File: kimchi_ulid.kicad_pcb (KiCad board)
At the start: 4 copper layers, 65 x 32 mm, 10 parts, among them J1 DF40HC(3.5)-60DS, J2 DF40HC(3.5)-60DS, K1 KIMCHI_MICRO, U1 24C32

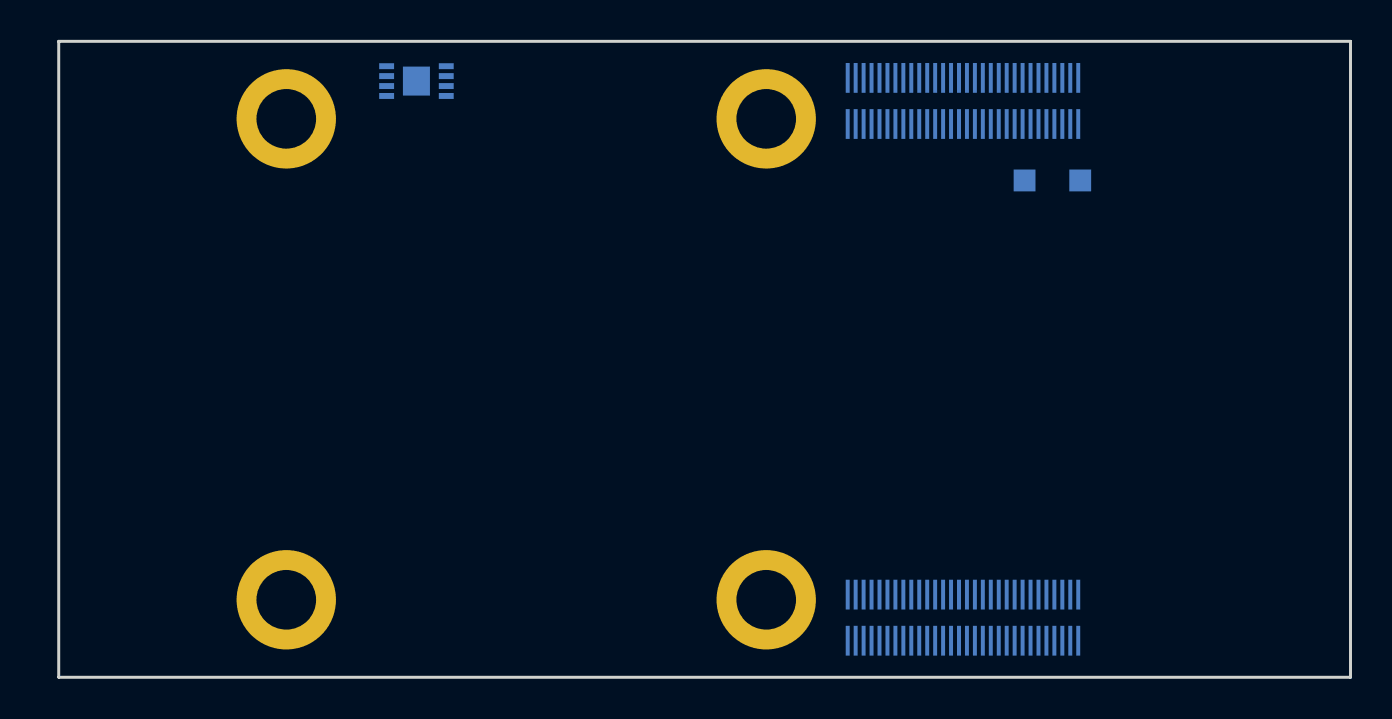
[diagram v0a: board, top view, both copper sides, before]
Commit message: Initial work on design
- Update symbols to KiCad v6
- Start inital placement and routing of design
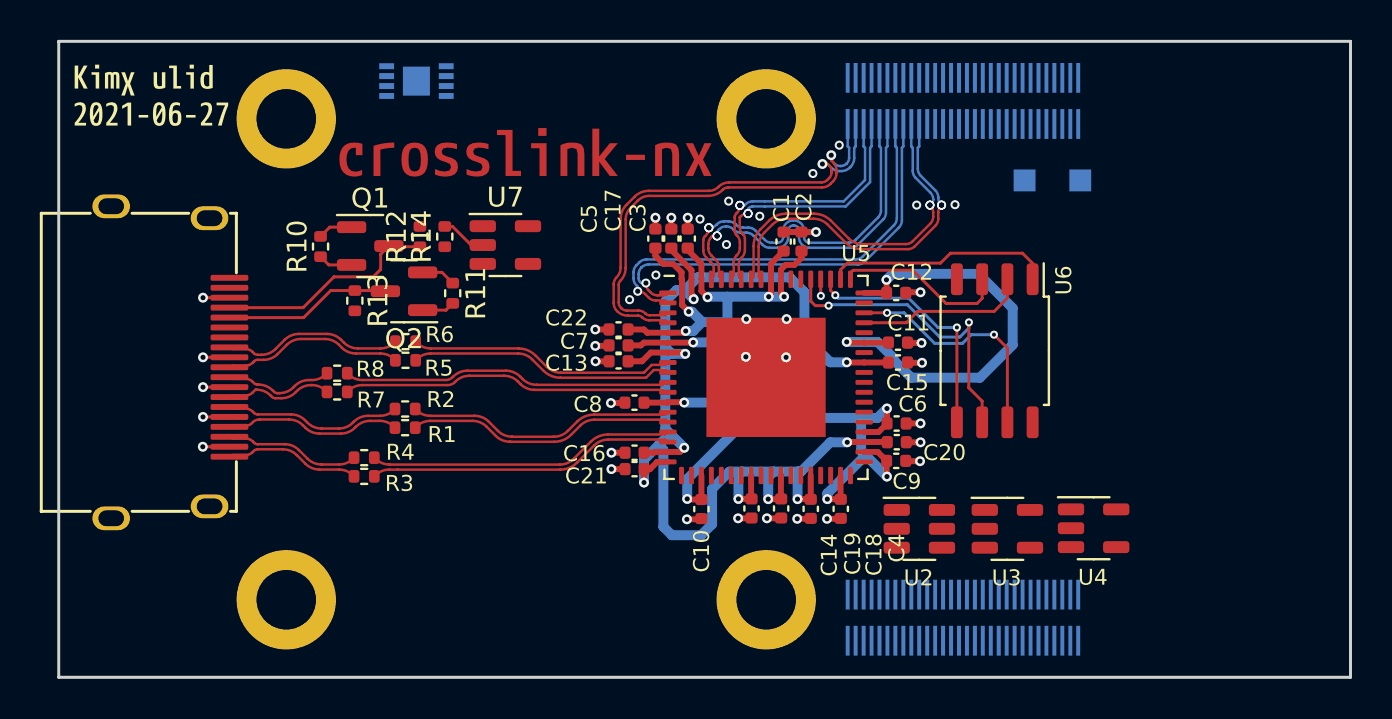
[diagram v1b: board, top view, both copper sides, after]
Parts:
- added C1: 0.1uF, Capacitor_SMD:C_0402_1005Metric, F.Cu at (143.5, 104.1)
- added C10: 0.1uF, Capacitor_SMD:C_0402_1005Metric, F.Cu at (139.3, 117.5)
- added C11: 0.1uF, Capacitor_SMD:C_0402_1005Metric, F.Cu at (149.2, 109.2)
- added C12: 0.1uF, Capacitor_SMD:C_0402_1005Metric, F.Cu at (149.1, 106.7)
- added C13: 0.1uF, Capacitor_SMD:C_0402_1005Metric, F.Cu at (135.2, 110.1)
- added C14: 0.1uF, Capacitor_SMD:C_0402_1005Metric, F.Cu at (141.9, 117.5)
- added C15: 0.1uF, Capacitor_SMD:C_0402_1005Metric, F.Cu at (149.2, 110.2)
- added C16: 0.1uF, Capacitor_SMD:C_0402_1005Metric, F.Cu at (136.0, 114.7)
- added C17: 0.1uF, Capacitor_SMD:C_0402_1005Metric, F.Cu at (137.8, 103.9)
- added C18: 0.1uF, Capacitor_SMD:C_0402_1005Metric, F.Cu at (144.8, 117.5)
- added C19: 0.1uF, Capacitor_SMD:C_0402_1005Metric, F.Cu at (143.3, 117.5)
- added C2: 0.1uF, Capacitor_SMD:C_0402_1005Metric, F.Cu at (144.4, 104.1)
- added C20: 0.1uF, Capacitor_SMD:C_0402_1005Metric, F.Cu at (149.2, 114.2)
- added C21: 0.1uF, Capacitor_SMD:C_0402_1005Metric, F.Cu at (136.0, 115.5)
- added C22: 0.1uF, Capacitor_SMD:C_0402_1005Metric, F.Cu at (135.2, 108.5)
- added C3: 0.1uF, Capacitor_SMD:C_0402_1005Metric, F.Cu at (138.7, 103.9)
- added C4: 0.1uF, Capacitor_SMD:C_0402_1005Metric, F.Cu at (146.3, 117.5)
- added C5: 0.1uF, Capacitor_SMD:C_0402_1005Metric, F.Cu at (137.0, 103.9)
- added C6: 0.1uF, Capacitor_SMD:C_0402_1005Metric, F.Cu at (149.2, 113.2)
- added C7: 0.1uF, Capacitor_SMD:C_0402_1005Metric, F.Cu at (135.2, 109.3)
- added C8: 0.1uF, Capacitor_SMD:C_0402_1005Metric, F.Cu at (136.0, 112.2)
- added C9: 0.1uF, Capacitor_SMD:C_0402_1005Metric, F.Cu at (149.1, 115.1)
- added J3: HDMI_A_1.4, kimchi_ulid:HDMI-10029449-111RLF, F.Cu at (114.6, 110.2)
- added Q1: 2N7002, Package_TO_SOT_SMD:SOT-23, F.Cu at (122.7, 104.3)
- added Q2: 2N7002, Package_TO_SOT_SMD:SOT-23, F.Cu at (124.4, 106.6)
- added R1: R, Resistor_SMD:R_0402_1005Metric, F.Cu at (124.4, 113.4)
- added R10: 2k2, Resistor_SMD:R_0402_1005Metric, F.Cu at (120.2, 104.3)
- added R11: 2k2, Resistor_SMD:R_0402_1005Metric, F.Cu at (126.8, 106.7)
- added R12: 2k2, Resistor_SMD:R_0402_1005Metric, F.Cu at (125.2, 103.8)
- added R13: 2k2, Resistor_SMD:R_0402_1005Metric, F.Cu at (121.9, 107.0)
- added R14: 47k, Resistor_SMD:R_0402_1005Metric, F.Cu at (126.4, 103.8)
- added R2: R, Resistor_SMD:R_0402_1005Metric, F.Cu at (124.4, 112.5)
- added R3: R, Resistor_SMD:R_0402_1005Metric, F.Cu at (122.4, 115.9)
- added R4: R, Resistor_SMD:R_0402_1005Metric, F.Cu at (122.4, 115.0)
- added R5: R, Resistor_SMD:R_0402_1005Metric, F.Cu at (124.5, 110.0)
- added R6: R, Resistor_SMD:R_0402_1005Metric, F.Cu at (124.5, 109.1)
- added R7: R, Resistor_SMD:R_0402_1005Metric, F.Cu at (121.0, 111.6)
- added R8: R, Resistor_SMD:R_0402_1005Metric, F.Cu at (121.0, 110.7)
- added U2: LM3880, Package_TO_SOT_SMD:SOT-23-6, F.Cu at (150.3, 118.5)
- added U3: LD3985M27R_SOT23, Package_TO_SOT_SMD:SOT-23-5, F.Cu at (154.7, 118.5)
- added U4: LD3985M27R_SOT23, Package_TO_SOT_SMD:SOT-23-5, F.Cu at (159.1, 118.5)
- added U5: LIFCL40-NX, Package_DFN_QFN:QFN-72-1EP_10x10mm_P0.5mm_EP6x6mm, F.Cu at (142.6, 110.9)
- added U6: W25Q32JVSS, Package_SO:SOIC-8_5.23x5.23mm_P1.27mm, F.Cu at (154.1, 109.6)
- added U7: 74AUC1G17, Package_TO_SOT_SMD:SOT-23-5, F.Cu at (129.5, 104.2)
- added svg2mod: G***, svg2mod, F.Cu at (111.3, 96.0)
- added svg2mod: G***, svg2mod, F.Cu at (111.7, 97.7)
- added svg2mod: G***, svg2mod, F.Cu at (130.4, 99.8)
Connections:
- D1 pad 2: (no net) -> /VCHG_PROT
- J1 pad 1: (no net) -> /USDHC3_CMD
- J1 pad 11: (no net) -> unconnected-(J1-Pad11)
- J1 pad 17: (no net) -> I2C3_SDA
- J1 pad 18: (no net) -> I2C3_SCL
- J1 pad 19: (no net) -> I2C2_SDA
- J1 pad 2: (no net) -> /USDHC3_CLK
- J1 pad 20: (no net) -> I2C2_SCL
- J1 pad 21: (no net) -> I2C1_SDA
- J1 pad 22: (no net) -> I2C1_SCL
- J1 pad 23: (no net) -> ECSPI1_SCLK
- J1 pad 24: (no net) -> ECSPI1_SS0
- J1 pad 25: (no net) -> ECSPI1_MOSI
- J1 pad 26: (no net) -> ECSPI1_MISO
- J1 pad 27: (no net) -> ECSPI2_SCLK
- J1 pad 28: (no net) -> ECSPI2_SS0
- J1 pad 29: (no net) -> ECSPI2_MOSI
- J1 pad 3: (no net) -> /USDHC3_DATA3
- J1 pad 30: (no net) -> ECSPI2_MISO
- J1 pad 31: (no net) -> /DISP_D0_N
- J1 pad 32: (no net) -> /DISP_D0_P
- J1 pad 33: (no net) -> /DISP_D1_N
- J1 pad 34: (no net) -> /DISP_D1_P
- J1 pad 35: (no net) -> /DISP_CK_N
- J1 pad 36: (no net) -> /DISP_CK_P
- J1 pad 37: (no net) -> /DISP_D2_N
- J1 pad 38: (no net) -> /DISP_D2_P
- J1 pad 39: (no net) -> /DISP_D3_N
- J1 pad 4: (no net) -> /USDHC3_DATA0
- J1 pad 40: (no net) -> /DISP_D3_P
- J1 pad 41: (no net) -> /CAM_D0_N
- J1 pad 42: (no net) -> /CAM_D0_P
- J1 pad 43: (no net) -> /CAM_D1_N
- J1 pad 44: (no net) -> /CAM_D1_P
- J1 pad 45: (no net) -> /CAM_CK_N
- J1 pad 46: (no net) -> /CAM_CK_P
- J1 pad 47: (no net) -> /CAM_D2_N
- J1 pad 48: (no net) -> /CAM_D2_P
- J1 pad 49: (no net) -> /CAM_D3_N
- J1 pad 5: (no net) -> /USDHC3_DATA1
- J1 pad 50: (no net) -> /CAM_D3_P
- J1 pad 51: (no net) -> unconnected-(J1-Pad51)
- J1 pad 57: (no net) -> USB2_VBUS
- J1 pad 58: (no net) -> USB2_ID
- J1 pad 59: (no net) -> USB2_DN
- J1 pad 6: (no net) -> /USDHC3_DATA2
- J1 pad 60: (no net) -> USB2_DP
- J2 pad 1: (no net) -> /ENET_MDIO
- J2 pad 10: (no net) -> /ENET_TD0
- J2 pad 11: (no net) -> /ENET_TD3
- J2 pad 12: (no net) -> /ENET_TD2
- J2 pad 13: (no net) -> /ENET_TX_CTL
- J2 pad 14: (no net) -> /ENET_TXC
- J2 pad 15: (no net) -> SAI2_RXD0
- J2 pad 16: (no net) -> SAI2_TXFS
- J2 pad 17: (no net) -> SAI2_RXC
- J2 pad 18: (no net) -> SAI2_TXD0
- J2 pad 19: (no net) -> SAI2_TXC
- J2 pad 2: (no net) -> /ENET_MDC
- J2 pad 20: (no net) -> SAI2_MCLK
- J2 pad 21: (no net) -> SAI2_RXFS
- J2 pad 22: (no net) -> GPIO1[15]
- J2 pad 23: (no net) -> GPIO1[14]
- J2 pad 24: (no net) -> GPIO1[13]
- J2 pad 25: (no net) -> GPIO1[12]
- J2 pad 26: (no net) -> GPIO1[11]
- J2 pad 27: (no net) -> GPIO1[10]
- J2 pad 28: (no net) -> GPIO1[9]
- J2 pad 29: (no net) -> GPIO1[1]
- J2 pad 3: (no net) -> /ENET_RD3
- J2 pad 30: (no net) -> GPIO1[0]
- J2 pad 31: (no net) -> SAI3_TXC
- J2 pad 32: (no net) -> SAI3_TXD
- J2 pad 33: (no net) -> SAI3_RXD
- J2 pad 34: (no net) -> SAI3_RXFS
- J2 pad 35: (no net) -> SAI3_RXC
- J2 pad 36: (no net) -> SAI3_TXFS
- J2 pad 37: (no net) -> SAI3_MCLK
- J2 pad 4: (no net) -> /ENET_RD1
- J2 pad 42: (no net) -> unconnected-(J2-Pad42)
- J2 pad 46: (no net) -> UART1_TX
- J2 pad 47: (no net) -> UART1_RX
- J2 pad 48: (no net) -> UART3_TX
- J2 pad 49: (no net) -> UART3_RX
- J2 pad 5: (no net) -> /ENET_RD2
- J2 pad 54: (no net) -> unconnected-(J2-Pad54)
- J2 pad 58: (no net) -> unconnected-(J2-Pad58)
- J2 pad 59: (no net) -> PCIE_USB_D_P
- J2 pad 6: (no net) -> /ENET_RD0
- J2 pad 60: (no net) -> PCIE_USB_D_N
- J2 pad 7: (no net) -> /ENET_RXC
- J2 pad 8: (no net) -> /ENET_RX_CTL
- J2 pad 9: (no net) -> /ENET_TD1
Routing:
- net +1V8: track 0.00 -> 69.6 mm, vias 0 -> 9
- net +1V0: track 0.00 -> 66.0 mm, vias 0 -> 11
- net /DISP_D0_P: track 0.00 -> 23.8 mm, vias 0 -> 1
- net /DISP_D0_N: track 0.00 -> 23.0 mm, vias 0 -> 1
- net +3V3: track 0.00 -> 22.8 mm, vias 0 -> 2
- net /DISP_D2_N: track 0.00 -> 22.0 mm, vias 0 -> 1
- net GND: track 0.00 -> 21.8 mm, vias 0 -> 40
- net /DISP_D2_P: track 0.00 -> 21.6 mm, vias 0 -> 1
- net /DISP_CK_P: track 0.00 -> 18.6 mm, vias 0 -> 2
- net /DISP_CK_N: track 0.00 -> 18.6 mm, vias 0 -> 2
- net /DISP_D3_P: track 0.00 -> 18.0 mm, vias 0 -> 2
- net /DISP_D3_N: track 0.00 -> 18.0 mm, vias 0 -> 2
- net /tmds_d0+: track 0.00 -> 16.3 mm
- net /tmds_d0-: track 0.00 -> 16.3 mm
- net /iCE_SCK: track 0.00 -> 15.6 mm, vias 0 -> 2
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- added copper zone on In1.Cu, net +1V8
- added copper zone on In2.Cu, net GND
- removed copper zone on In1.Cu, net GND
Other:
- net class CSI/DSI removed
- net class Default removed
- net class PCIE removed
- net class USB removed

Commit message: Update routing
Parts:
- added C23: C, Capacitor_SMD:C_0402_1005Metric, F.Cu at (149.9, 100.9)
- added C24: 4.7uF, Capacitor_SMD:C_0603_1608Metric, F.Cu at (164.6, 97.2)
- added C25: 4.7uF, Capacitor_SMD:C_0603_1608Metric, F.Cu at (159.7, 97.2)
- added C26: 4.7uF, Capacitor_SMD:C_0603_1608Metric, F.Cu at (154.7, 97.2)
- added C27: 0.01uF, Capacitor_SMD:C_0402_1005Metric, F.Cu at (161.8, 100.4)
- added C28: 0.01uF, Capacitor_SMD:C_0402_1005Metric, F.Cu at (156.8, 100.3)
- added C29: 0.01uF, Capacitor_SMD:C_0402_1005Metric, F.Cu at (151.9, 100.3)
- added C30: 0.1uF, Capacitor_SMD:C_0402_1005Metric, F.Cu at (153.4, 114.8)
- added C31: 10uF, Capacitor_SMD:C_0603_1608Metric, F.Cu at (164.6, 100.2)
- added C32: 10uF, Capacitor_SMD:C_0603_1608Metric, F.Cu at (154.6, 100.1)
- added C33: 10uF, Capacitor_SMD:C_0603_1608Metric, F.Cu at (159.6, 100.1)
- added C34: 0.1uF, Capacitor_SMD:C_0402_1005Metric, F.Cu at (132.4, 103.5)
- added C35: 0.1uF, Capacitor_SMD:C_0402_1005Metric, F.Cu at (132.4, 105.3)
- added J4: Jtag, Connector_PinHeader_2.54mm:PinHeader_1x07_P2.54mm_Vertical, F.Cu at (167.2, 118.5)
- added J5: Flash, Connector_PinHeader_2.54mm:PinHeader_1x07_P2.54mm_Vertical, F.Cu at (160.7, 118.5)
- added R15: 100R, Resistor_SMD:R_0402_1005Metric, F.Cu at (121.5, 107.8)
- added R16: R, Resistor_SMD:R_0402_1005Metric, F.Cu at (147.9, 100.9)
- added U10: TPD4E02B04DQA, Package_SON:USON-10_2.5x1.0mm_P0.5mm, F.Cu at (118.3, 110.7)
- added U11: LD3985M27R_SOT23, Package_TO_SOT_SMD:SOT-23-5, F.Cu at (152.2, 97.8)
- added U8: 74LVC1G125, Package_TO_SOT_SMD:SOT-23-5, F.Cu at (129.5, 103.4)
- added U9: TPD4E02B04DQA, Package_SON:USON-10_2.5x1.0mm_P0.5mm, F.Cu at (118.3, 113.7)
- D1: moved to F.Cu
- U7: value 74AUC1G17 -> 74LVC2G17; footprint Package_TO_SOT_SMD:SOT-23-5 -> Package_TO_SOT_SMD:SOT-23-6
- moved U3 22.0 mm to (162.1, 97.8), turned to -90 degrees
- moved U4 20.8 mm to (157.1, 97.8), turned to -90 degrees
- moved U2 20.3 mm to (148.7, 98.3), turned to 90 degrees
- moved D1 10.0 mm to (166.6, 98.0), turned to 90 degrees
- moved U7 2.50 mm to (129.5, 106.8), turned to 180 degrees
- moved R13 0.48 mm to (121.5, 106.8), turned to 180 degrees
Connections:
- net Net-(J3-Pad18) renamed VDD
- J3 pad 13: unconnected-(J3-Pad13) -> Net-(J3-Pad13)
- U2 pad 1: unconnected-(U2-Pad1) -> VDD_3V3
- U2 pad 2: unconnected-(U2-Pad2) -> GND
- U2 pad 3: unconnected-(U2-Pad3) -> Net-(U2-Pad3)
- U2 pad 4: unconnected-(U2-Pad4) -> /en2
- U2 pad 5: unconnected-(U2-Pad5) -> /en1
- U2 pad 6: unconnected-(U2-Pad6) -> /en0
- U3 pad 3: unconnected-(U3-Pad3) -> /en0
- U3 pad 4: unconnected-(U3-Pad4) -> Net-(U3-Pad4)
- U4 pad 3: unconnected-(U4-Pad3) -> /en1
- U4 pad 4: unconnected-(U4-Pad4) -> Net-(U4-Pad4)
- U5 pad 24: unconnected-(U5-Pad24) -> Net-(U5-Pad24)
- U5 pad 25: unconnected-(U5-Pad25) -> Net-(U5-Pad25)
- U5 pad 27: unconnected-(U5-Pad27) -> Net-(U5-Pad27)
- U7 pad 1: (no net) -> Net-(R15-Pad2)
- U7 pad 2: Net-(J3-Pad19) -> GND
- U7 pad 3: GND -> Net-(J3-Pad19)
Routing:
- net GND: track 21.8 -> 52.6 mm, vias 40 -> 55
- net I2C4_SDA: track 0.00 -> 27.8 mm
- net I2C4_SCL: track 0.00 -> 27.2 mm
- net VDD: track 0.00 -> 24.4 mm, vias 0 -> 4
- net VDD_3V3: track 0.00 -> 18.7 mm, vias 0 -> 4
- net Net-(J3-Pad19): track 2.30 -> 18.7 mm
- net /en0: track 0.00 -> 15.6 mm
- net Net-(R15-Pad2): track 0.00 -> 14.5 mm
- net /en1: track 0.00 -> 9.40 mm
- net VDD_5V: track 0.00 -> 8.74 mm, vias 0 -> 1
- net +1V8: track 69.6 -> 76.8 mm, vias 9 -> 11
- net Net-(J3-Pad13): track 0.00 -> 5.81 mm
- net +1V0: track 66.0 -> 69.0 mm
- net +3V3: track 22.8 -> 25.7 mm
- net /en2: track 0.00 -> 2.90 mm
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- added copper zone on B.Cu, net +1V8
- added copper zone on F.Cu, net GND
- removed copper zone on B.Cu, net GND

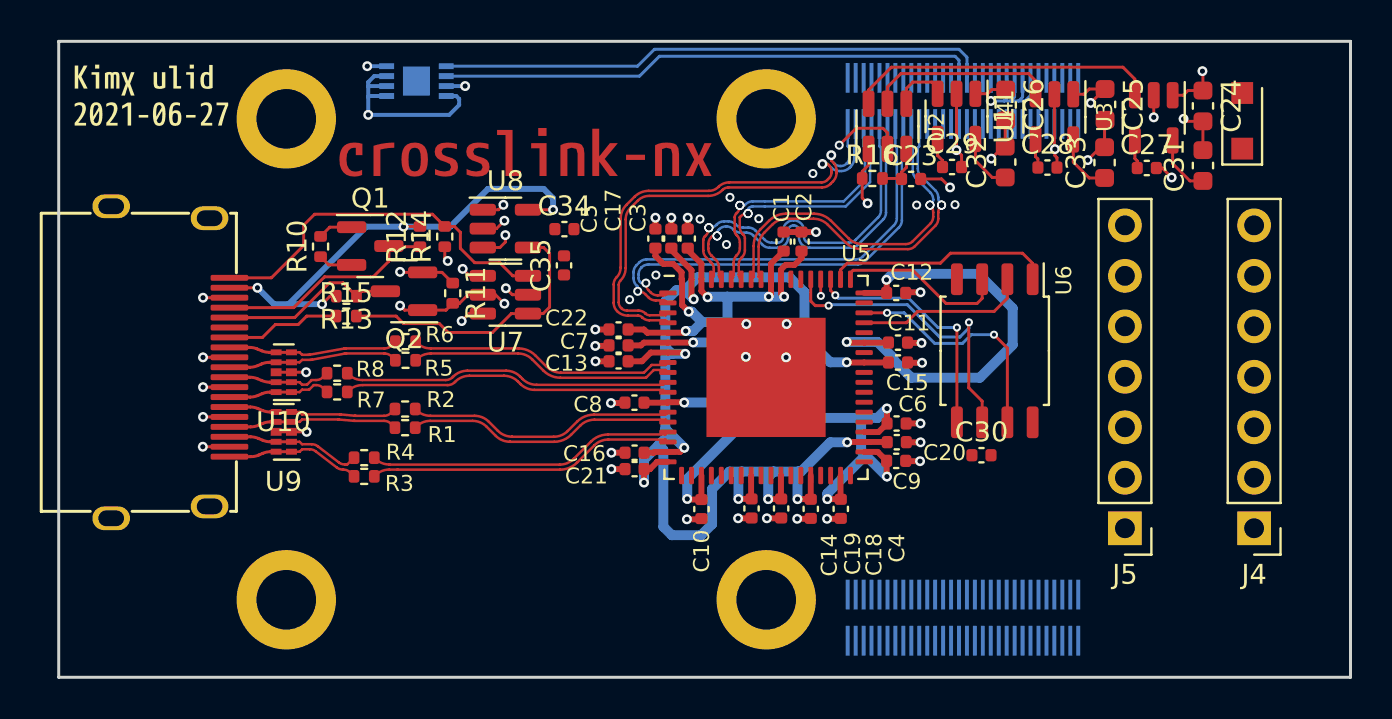
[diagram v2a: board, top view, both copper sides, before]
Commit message: Update
- Complete inital routing
- Render a board view and update readme
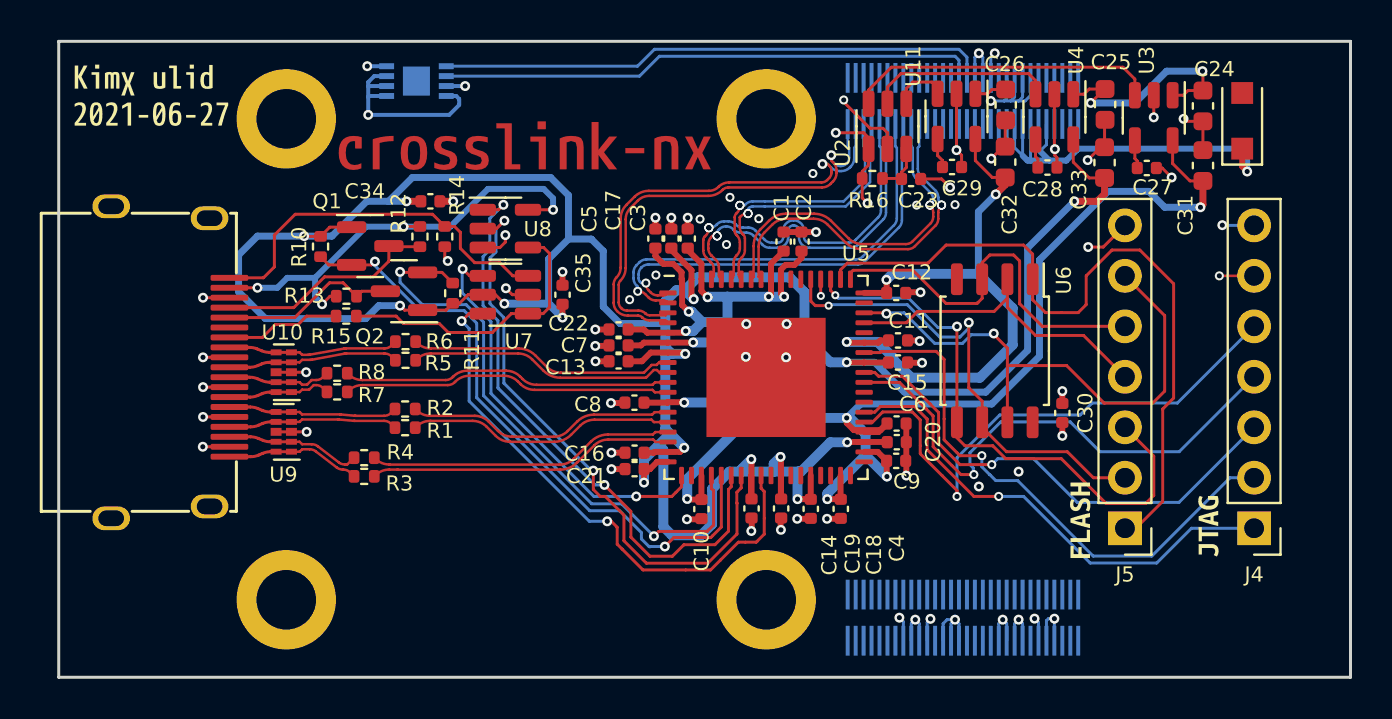
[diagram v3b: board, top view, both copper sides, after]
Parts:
- added svg2mod: G***, svg2mod, F.Cu at (164.8, 118.4)
- added svg2mod: G***, svg2mod, F.Cu at (158.4, 118.1)
- moved C34 6.89 mm to (125.7, 102.0)
- moved C30 4.59 mm to (157.5, 112.7), turned to -90 degrees
- moved C35 1.48 mm to (132.3, 106.8)
- moved svg2mod 0.34 mm to (130.4, 99.4)
- moved C11 0.11 mm to (149.2, 109.0)
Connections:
- J4 pad 1: unconnected-(J4-Pad1) -> /IO
- J4 pad 2: unconnected-(J4-Pad2) -> /TMS
- J4 pad 3: unconnected-(J4-Pad3) -> /TDI
- J4 pad 4: unconnected-(J4-Pad4) -> /TDO
- J4 pad 5: unconnected-(J4-Pad5) -> /TCK
- J4 pad 6: unconnected-(J4-Pad6) -> GND
- J4 pad 7: GND -> +3V3
- U5 pad 41: unconnected-(U5-Pad41) -> /TCK
- U5 pad 42: unconnected-(U5-Pad42) -> /IO
- U5 pad 45: unconnected-(U5-Pad45) -> /TDO
- U5 pad 46: unconnected-(U5-Pad46) -> /TDI
- U5 pad 48: unconnected-(U5-Pad48) -> /TMS
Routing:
- net +1V8: track 76.8 -> 149.8 mm, vias 11 -> 15
- net Net-(Q1-Pad2): track 1.73 -> 31.9 mm, vias 0 -> 2
- net Net-(U5-Pad25): track 1.25 -> 30.5 mm, vias 1 -> 2
- net Net-(U5-Pad24): track 1.14 -> 30.3 mm, vias 1 -> 2
- net /TMS: track 0.00 -> 28.2 mm, vias 0 -> 1
- net +1V0: track 69.0 -> 97.0 mm, vias 11 -> 12
- net /TCK: track 0.00 -> 27.5 mm, vias 0 -> 1
- net Net-(U5-Pad27): track 1.22 -> 28.0 mm, vias 1 -> 2
- net /TDO: track 0.00 -> 26.7 mm, vias 0 -> 1
- net Net-(Q2-Pad2): track 2.88 -> 29.4 mm, vias 1 -> 2
- net /FLASH_CS: track 11.5 -> 37.0 mm
- net /TDI: track 0.00 -> 25.1 mm, vias 0 -> 1
- net /IO: track 0.00 -> 24.6 mm, vias 0 -> 1
- net VCHG: track 0.00 -> 23.3 mm, vias 0 -> 1
- net VDD_3V3: track 18.7 -> 39.8 mm, vias 4 -> 7
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- added copper zone on B.Cu, net +3V3
- added copper zone on In1.Cu, net +3V3
- removed copper zone on B.Cu, net +1V8
- removed copper zone on In1.Cu, net +1V8
